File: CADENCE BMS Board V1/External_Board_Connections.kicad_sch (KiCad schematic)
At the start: 50 parts, among them J10 Conn_01x08, J11 Conn_01x06, J12 Conn_01x02, J13 Conn_01x08, J14 Conn_01x04, J15 Conn_01x08, J2 Conn_01x02, J27 USB_C_Receptacle_USB2.0_16P, J28 Conn_01x02, J29 Conn_01x02, J3 Conn_01x08, J30 Conn_01x02, J31 Conn_01x04, J4 Conn_01x02, J5 Conn_01x01_Socket, J6 Conn_01x01_Socket, J7 Conn_01x01_Socket, J8 Conn_01x01_Socket, J9 Conn_01x04, Q27 Q_PMOS_DGS, Q28 Q_PMOS_DGS, U11 CYPD3177-24LQ

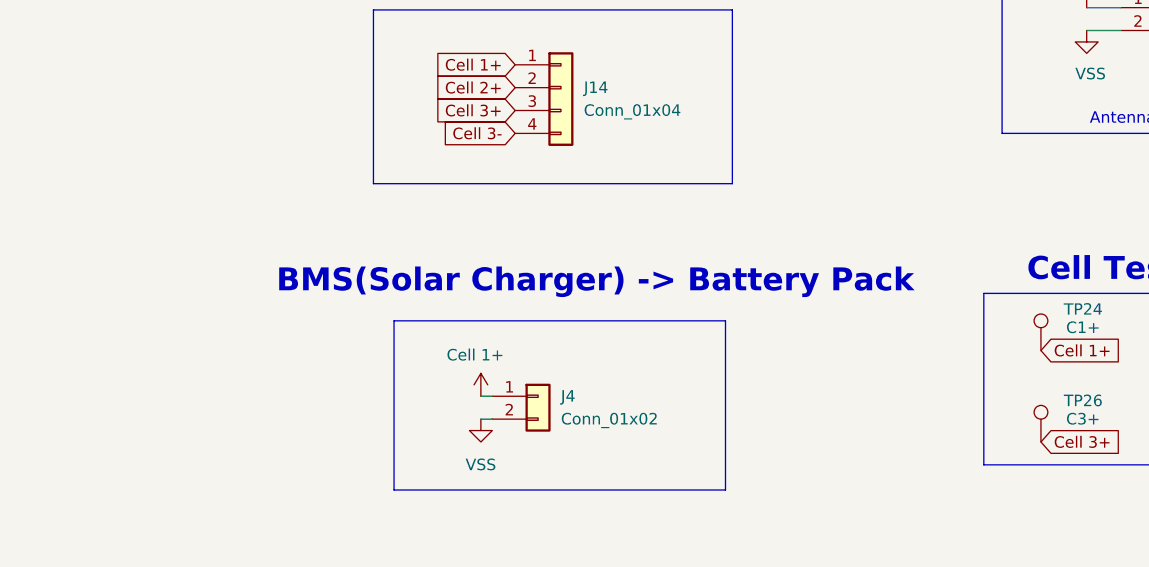
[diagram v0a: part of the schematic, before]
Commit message: Updates to CON footprints and out of stock components for JLC
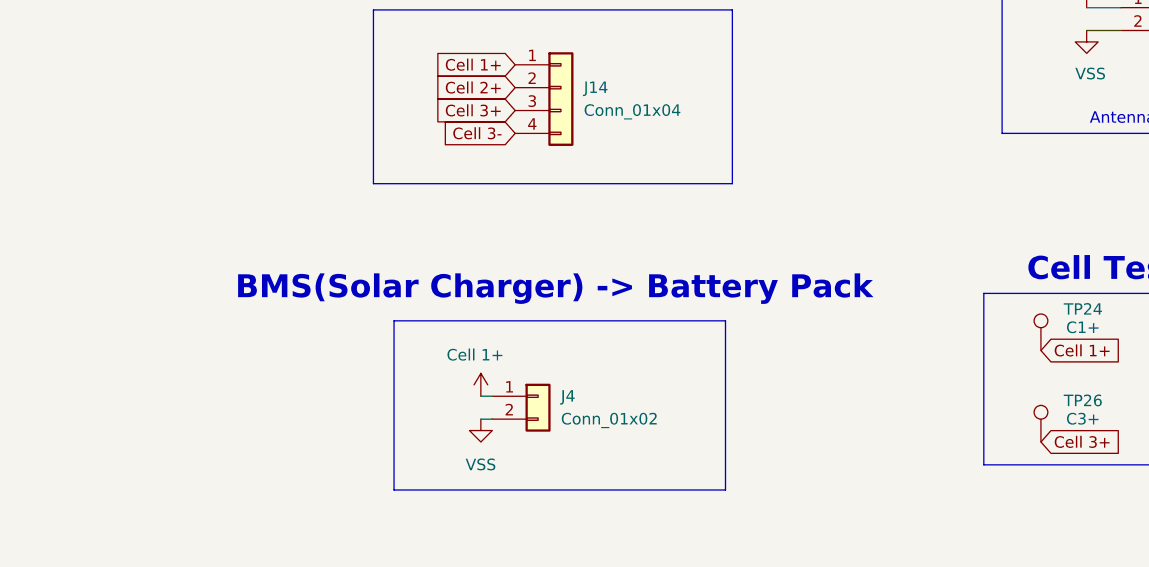
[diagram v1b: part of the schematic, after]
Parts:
- J14: footprint Connector_Samtec_HPM_THT:Samtec_HPM-04-05-x-S_Straight_1x04_Pitch5.08mm -> JST_4Pin_CON:LC04T
- J29, J30: footprint Connector_JST:JST_NV_B02P-NV_1x02_P5.00mm_Vertical -> JST_CON:SHDR2W120P580X500_2X1_790X1380X1460P
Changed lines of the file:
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@@
 	(text "BMS(Solar Charger) -> Battery Pack\n"
 		(exclude_from_sim no)
-		(at 313.69 119.38 0)
+		(at 309.118 120.142 0)
 		(effects
 			(font
@@
 			)
 		)
-		(property "Footprint" "Connector_JST:JST_NV_B02P-NV_1x02_P5.00mm_Vertical"
+		(property "Footprint" "JST_CON:SHDR2W120P580X500_2X1_790X1380X1460P"
 			(at 377.19 88.9 0)
 			(hide yes)
@@
 			)
 		)
-		(property "Footprint" "Connector_Samtec_HPM_THT:Samtec_HPM-04-05-x-S_Straight_1x04_Pitch5.08mm"
+		(property "Footprint" "JST_4Pin_CON:LC04T"
 			(at 309.88 97.79 0)
 			(hide yes)
@@
 			)
 		)
-		(property "Footprint" "Connector_JST:JST_NV_B02P-NV_1x02_P5.00mm_Vertical"
+		(property "Footprint" "JST_CON:SHDR2W120P580X500_2X1_790X1380X1460P"
 			(at 379.73 72.39 0)
 			(hide yes)

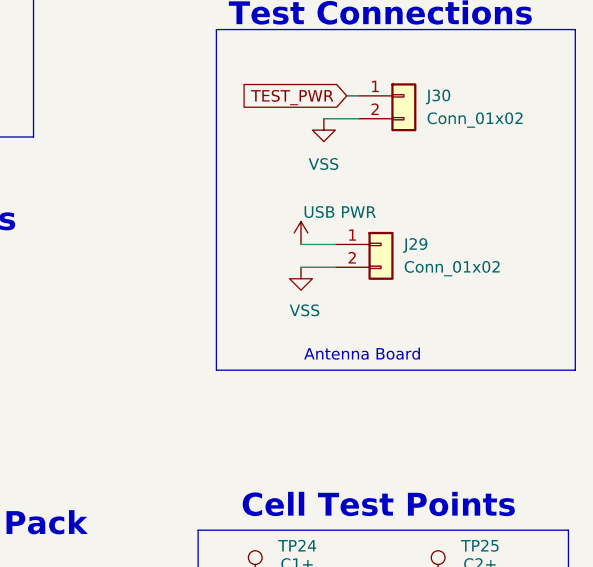
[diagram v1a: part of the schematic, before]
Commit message: Updated for an error found with Power good alert
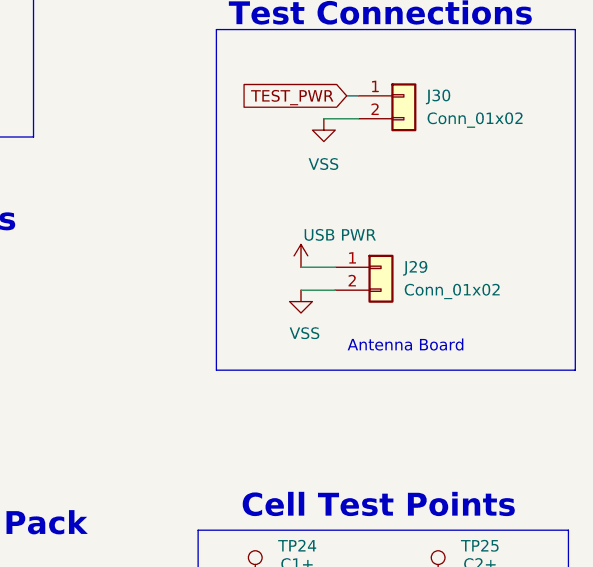
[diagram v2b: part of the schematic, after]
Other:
- moved on the sheet: J29
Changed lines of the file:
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@@
 	(text "Antenna Board"
 		(exclude_from_sim no)
-		(at 375.158 101.346 0)
+		(at 379.984 100.33 0)
 		(effects
 			(font
@@
 	(wire
 		(pts
-			(xy 368.3 88.9) (xy 372.11 88.9)
+			(xy 368.3 91.44) (xy 372.11 91.44)
 		)
 		(stroke
@@
 	(wire
 		(pts
-			(xy 368.3 91.44) (xy 372.11 91.44)
+			(xy 368.3 93.98) (xy 372.11 93.98)
 		)
 		(stroke
@@
 	(symbol
 		(lib_id "Connector_Generic:Conn_01x02")
-		(at 377.19 88.9 0)
+		(at 377.19 91.44 0)
 		(unit 1)
 		(body_style 1)
@@
 		(fields_autoplaced yes)
 		(property "Reference" "J29"
-			(at 379.73 88.8999 0)
+			(at 379.73 91.4399 0)
 			(show_name no)
 			(do_not_autoplace no)
@@
 		)
 		(property "Value" "Conn_01x02"
-			(at 379.73 91.4399 0)
+			(at 379.73 93.9799 0)
 			(show_name no)
 			(do_not_autoplace no)
@@
 		)
 		(property "Footprint" "JST_CON:SHDR2W120P580X500_2X1_790X1380X1460P"
-			(at 377.19 88.9 0)
+			(at 377.19 91.44 0)
 			(hide yes)
 			(show_name no)
@@
 		)
 		(property "Datasheet" ""
-			(at 377.19 88.9 0)
+			(at 377.19 91.44 0)
 			(hide yes)
 			(show_name no)
@@
 		)
 		(property "Description" "Generic connector, single row, 01x02, script generated (kicad-library-utils/schlib/autogen/connector/)"
-			(at 377.19 88.9 0)
+			(at 377.19 91.44 0)
 			(hide yes)
 			(show_name no)
@@
 		)
 		(property "LCSC" ""
-			(at 377.19 88.9 0)
+			(at 377.19 91.44 0)
 			(hide yes)
 			(show_name no)
@@
 		)
 		(property "Sim.Type" ""
-			(at 377.19 88.9 0)
+			(at 377.19 91.44 0)
 			(hide yes)
 			(show_name no)
@@
 		)
 		(property "Voltage" ""
-			(at 377.19 88.9 0)
+			(at 377.19 91.44 0)
 			(hide yes)
 			(show_name no)
@@
 	(symbol
 		(lib_id "power:GND")
-		(at 368.3 91.44 0)
+		(at 368.3 93.98 0)
 		(unit 1)
 		(body_style 1)
@@
 		(dnp no)
 		(property "Reference" "#PWR082"
-			(at 368.3 97.79 0)
+			(at 368.3 100.33 0)
 			(hide yes)
 			(show_name no)
@@
 		)
 		(property "Value" "VSS"
-			(at 367.03 96.266 0)
+			(at 367.03 98.806 0)
 			(show_name no)
 			(do_not_autoplace no)
@@
 		)
 		(property "Footprint" ""
-			(at 368.3 91.44 0)
+			(at 368.3 93.98 0)
 			(hide yes)
 			(show_name no)
@@
 		)
 		(property "Datasheet" ""
-			(at 368.3 91.44 0)
+			(at 368.3 93.98 0)
 			(hide yes)
 			(show_name no)
@@
 		)
 		(property "Description" "Power symbol creates a global label with name \"GND\" , ground"
-			(at 368.3 91.44 0)
+			(at 368.3 93.98 0)
 			(hide yes)
 			(show_name no)
@@
 	(symbol
 		(lib_id "power:+3.3V")
-		(at 368.3 88.9 0)
+		(at 368.3 91.44 0)
 		(unit 1)
 		(body_style 1)
@@
 		(dnp no)
 		(property "Reference" "#PWR074"
-			(at 368.3 92.71 0)
+			(at 368.3 95.25 0)
 			(hide yes)
 			(show_name no)
@@
 		)
 		(property "Value" "USB PWR"
-			(at 368.554 85.344 0)
+			(at 368.554 87.884 0)
 			(show_name no)
 			(do_not_autoplace no)
@@
 		)
 		(property "Footprint" ""
-			(at 368.3 88.9 0)
+			(at 368.3 91.44 0)
 			(hide yes)
 			(show_name no)
@@
 		)
 		(property "Datasheet" ""
-			(at 368.3 88.9 0)
+			(at 368.3 91.44 0)
 			(hide yes)
 			(show_name no)
@@
 		)
 		(property "Description" "Power symbol creates a global label with name \"+3.3V\""
-			(at 368.3 88.9 0)
+			(at 368.3 91.44 0)
 			(hide yes)
 			(show_name no)

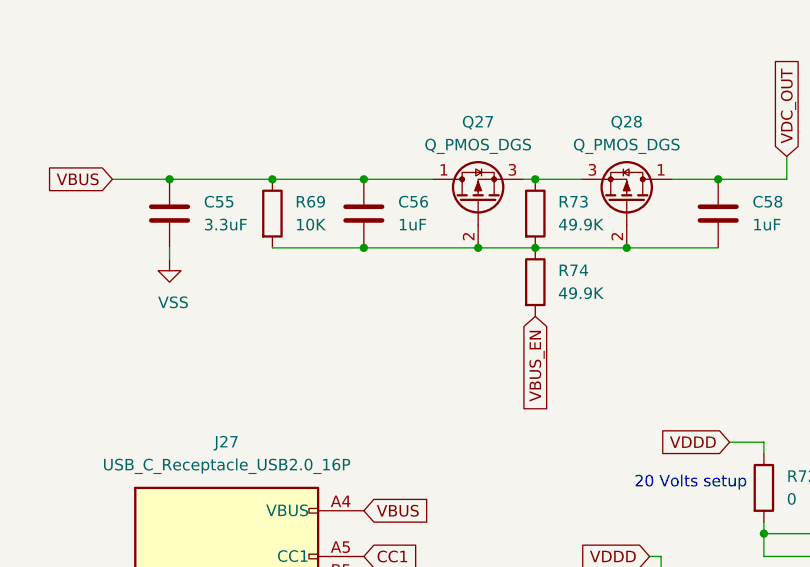
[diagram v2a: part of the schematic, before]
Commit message: Updates to Schematic
Found an error with power delivery USB-C and with the solar charger
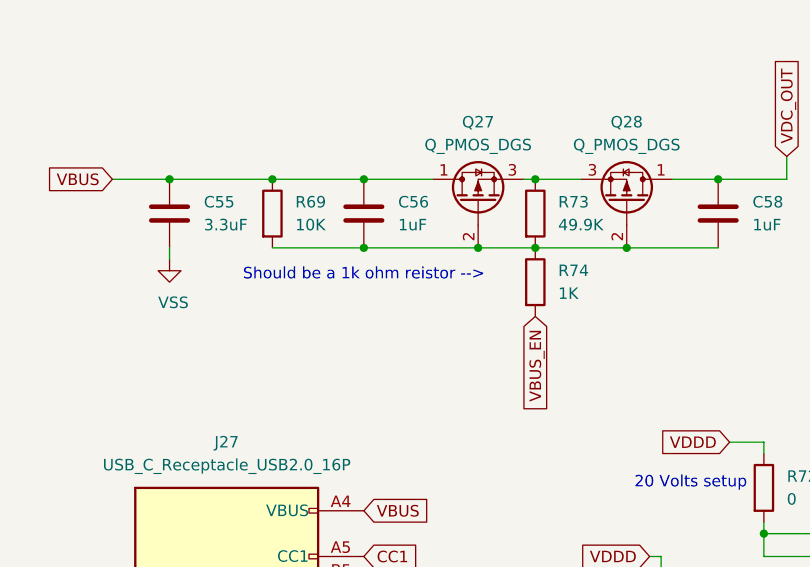
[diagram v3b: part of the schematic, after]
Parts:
- R74: value 49.9K -> 1K
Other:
- note added: "Should be a 1k ohm reistor -->"
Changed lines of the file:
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@@
 		)
 	)
+	(text "Should be a 1k ohm reistor -->"
+		(exclude_from_sim no)
+		(at 85.09 193.548 0)
+		(effects
+			(font
+				(size 1.27 1.27)
+			)
+		)
+	)
 	(text "USB-C Power Delivery"
 		(exclude_from_sim no)
@@
 			)
 		)
-		(property "Value" "49.9K"
+		(property "Value" "1K"
 			(at 106.68 195.5799 0)
 			(show_name no)

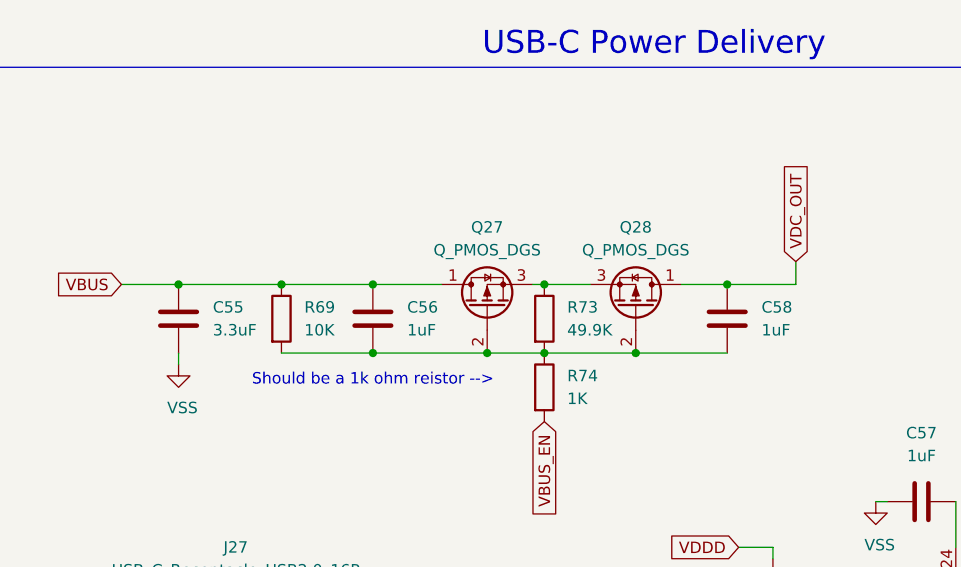
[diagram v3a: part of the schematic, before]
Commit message: Troubleshooting Notes on things to change for next revision
Updates to the Solar charger to ensure it powers on and updates to USB-C schematic fixing an error with the pinouts of the p channel FETS
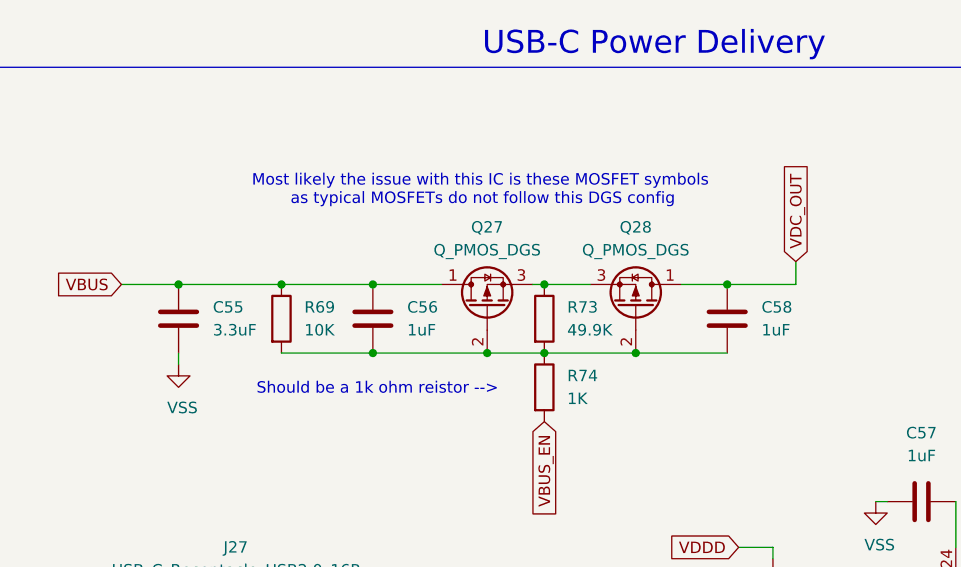
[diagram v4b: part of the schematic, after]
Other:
- note added: "Most likely the issue with this IC is these MOSFET symbols as typical MOSFETs do not follow this DGS config"
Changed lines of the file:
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@@
+		)
+	)
+	(text "Most likely the issue with this IC is these MOSFET symbols\n as typical MOSFETs do not follow this DGS config"
+		(exclude_from_sim no)
+		(at 97.028 172.466 0)
+		(effects
+			(font
+				(size 1.27 1.27)
+			)
 		)
 	)
@@
 	(text "Should be a 1k ohm reistor -->"
 		(exclude_from_sim no)
-		(at 85.09 193.548 0)
+		(at 85.598 194.564 0)
 		(effects
 			(font

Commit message: Adding in a connector for burn wire
Comms requested a burn wire connector that can supply the nominal 10.8V. This change will mark the start of the second version of the BMS board
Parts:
- added J32: Conn_01x02, Connector_JST:JST_XH_B2B-XH-A_1x02_P2.50mm_Vertical, symbol Connector_Generic:Conn_01x02
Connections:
- net UNREG: now also J32.1 (Pin_1)
- net VSS: now also J32.2 (Pin_2)
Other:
- note added: "Antenna Board Burn Wire"
- moved on the sheet: J29
